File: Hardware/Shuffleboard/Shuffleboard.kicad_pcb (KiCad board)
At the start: 4 copper layers, 130 x 131.5 mm, 47 parts, among them IC1 DG3157EDL-T1-GE3, IC2 DG3157EDL-T1-GE3, J1 1869279, J2 1869279, J3 Conn_01x10, Q1 NMOS, U1 COM-09032, U2 PAM8302AAS, U3 LMV331

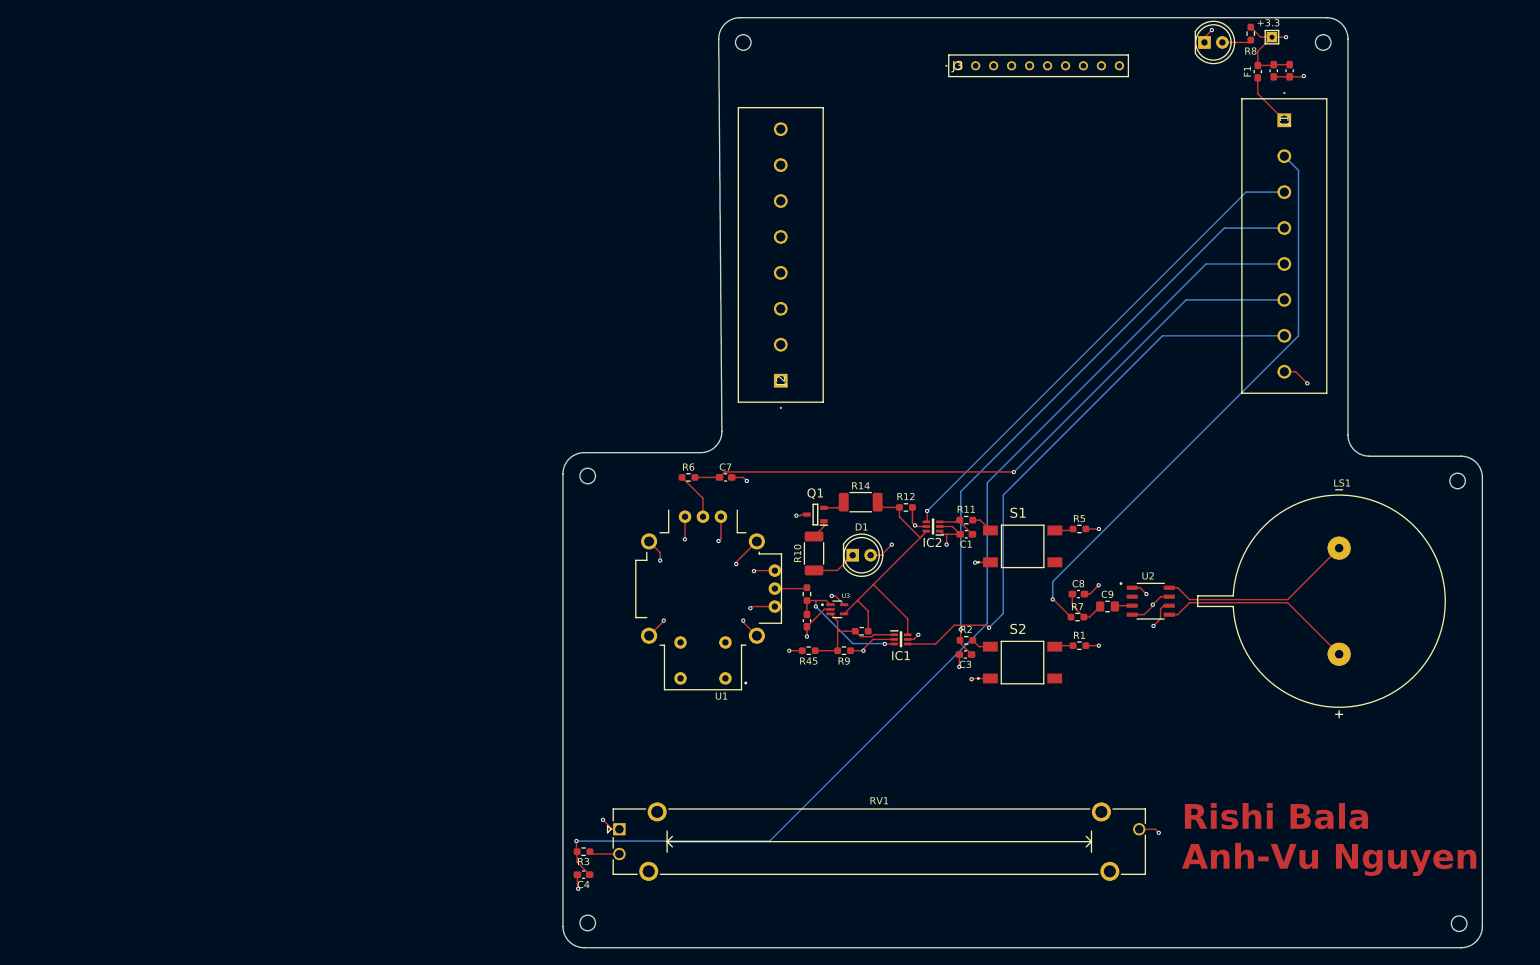
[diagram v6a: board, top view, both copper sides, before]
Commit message: footprints, tracing
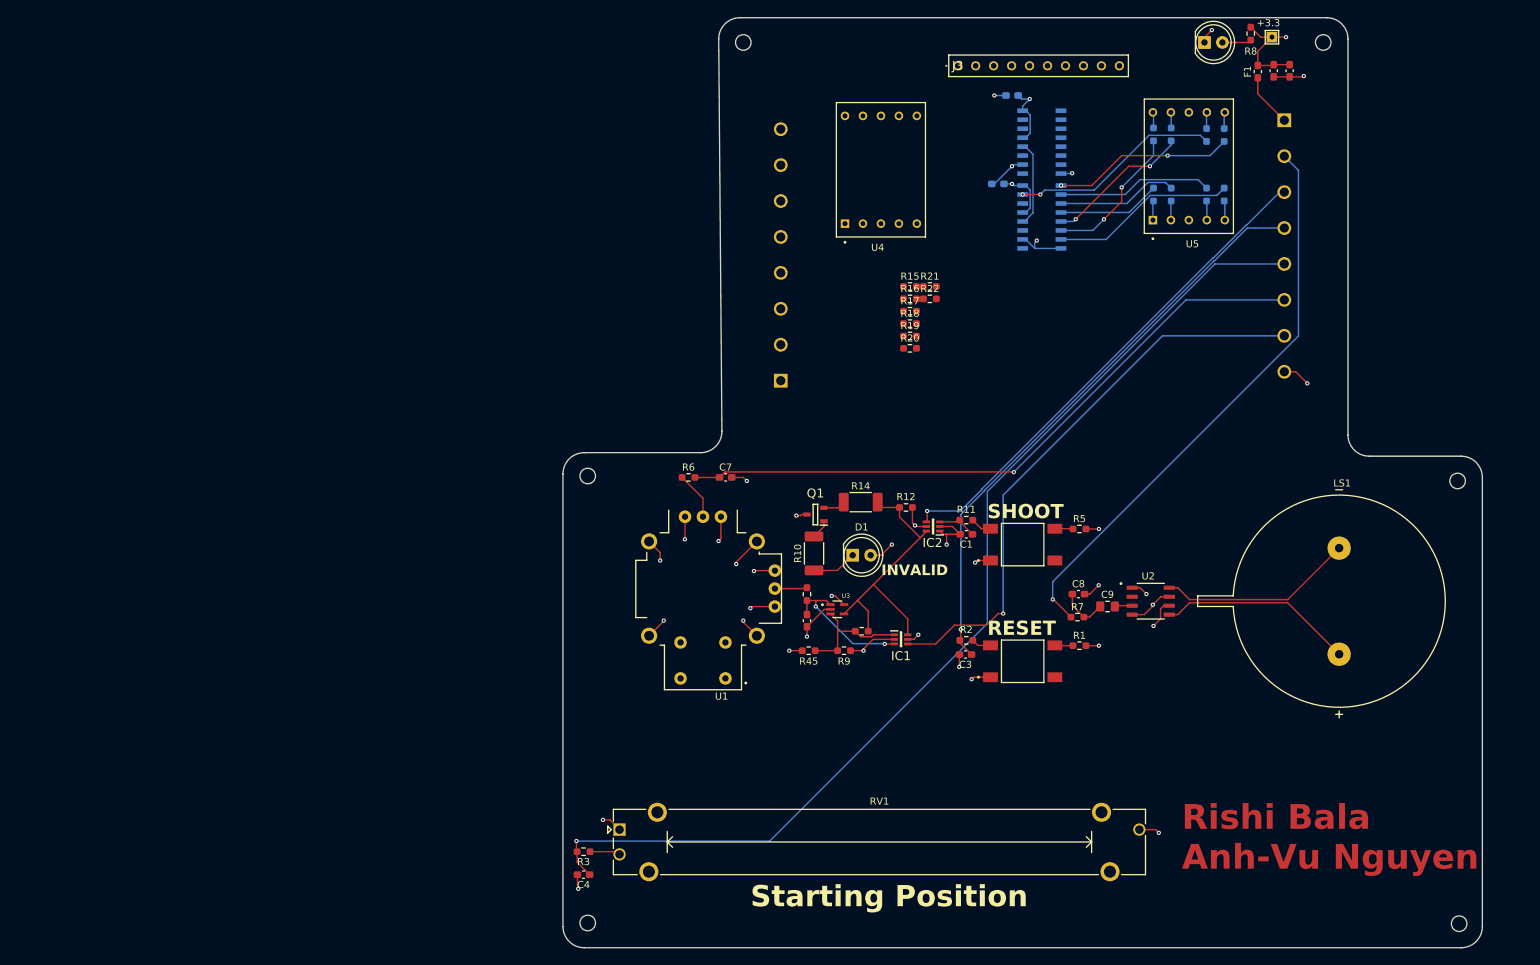
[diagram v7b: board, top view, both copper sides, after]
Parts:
- added C10: 100n, Capacitor_SMD:C_0603_1608Metric_Pad1.08x0.95mm_HandSolder, B.Cu at (173.5, 36.0)
- added C11: 100n, Capacitor_SMD:C_0603_1608Metric_Pad1.08x0.95mm_HandSolder, B.Cu at (171.5, 48.5)
- added R15: 100, Resistor_SMD:R_0603_1608Metric_Pad0.98x0.95mm_HandSolder, F.Cu at (159.1, 63.0)
- added R16: 100, Resistor_SMD:R_0603_1608Metric_Pad0.98x0.95mm_HandSolder, F.Cu at (159.1, 64.8)
- added R17: 100, Resistor_SMD:R_0603_1608Metric_Pad0.98x0.95mm_HandSolder, F.Cu at (159.1, 66.5)
- added R18: 100, Resistor_SMD:R_0603_1608Metric_Pad0.98x0.95mm_HandSolder, F.Cu at (159.1, 68.2)
- added R19: 100, Resistor_SMD:R_0603_1608Metric_Pad0.98x0.95mm_HandSolder, F.Cu at (159.1, 70.0)
- added R20: 100, Resistor_SMD:R_0603_1608Metric_Pad0.98x0.95mm_HandSolder, F.Cu at (159.1, 71.8)
- added R21: 100, Resistor_SMD:R_0603_1608Metric_Pad0.98x0.95mm_HandSolder, F.Cu at (161.9, 63.0)
- added R22: 100, Resistor_SMD:R_0603_1608Metric_Pad0.98x0.95mm_HandSolder, F.Cu at (161.9, 64.8)
- added R23: 100, Resistor_SMD:R_0603_1608Metric_Pad0.98x0.95mm_HandSolder, B.Cu at (201.0, 41.6)
- added R24: 100, Resistor_SMD:R_0603_1608Metric_Pad0.98x0.95mm_HandSolder, B.Cu at (203.5, 41.6)
- added R25: 100, Resistor_SMD:R_0603_1608Metric_Pad0.98x0.95mm_HandSolder, B.Cu at (201.0, 50.0)
- added R26: 100, Resistor_SMD:R_0603_1608Metric_Pad0.98x0.95mm_HandSolder, B.Cu at (196.0, 50.0)
- added R27: 100, Resistor_SMD:R_0603_1608Metric_Pad0.98x0.95mm_HandSolder, B.Cu at (193.5, 50.0)
- added R28: 100, Resistor_SMD:R_0603_1608Metric_Pad0.98x0.95mm_HandSolder, B.Cu at (196.0, 41.5)
- added R29: 100, Resistor_SMD:R_0603_1608Metric_Pad0.98x0.95mm_HandSolder, B.Cu at (193.5, 41.5)
- added R30: 100, Resistor_SMD:R_0603_1608Metric_Pad0.98x0.95mm_HandSolder, B.Cu at (203.5, 50.0)
- added U4: INND-TS56RCB, ShuffleboardFootprints:LED_INND-TS56RCB, F.Cu at (155.0, 46.5)
- added U5: INND-TS56RCB, ShuffleboardFootprints:LED_INND-TS56RCB, F.Cu at (198.5, 46.0)
- added U6: LOGIC-74HC595N_DIP16_, ShuffleboardFootprints:SOIC127P600X175-16N, B.Cu at (177.7, 42.6)
- added U8: LOGIC-74HC595N_DIP16_, ShuffleboardFootprints:SOIC127P600X175-16N, B.Cu at (177.7, 53.2)
- J1, J2: footprint ShuffleboardFootprints:1869279 -> Footprint:1869279; moved to B.Cu
- moved S1 0.25 mm to (175.0, 99.5)
- moved S2 0.18 mm to (175.0, 116.0)
- moved RV1 0.05 mm to (118.0, 139.8)
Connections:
- J2 pad 1: unconnected-(J2-Pad1) -> /Connector/PB8_MOSI(PICO)
- J2 pad 2: unconnected-(J2-Pad2) -> /Connector/PB9_SPI_CLK
- J2 pad 3: unconnected-(J2-Pad3) -> /Connector/PB16_LATCH_PULSE
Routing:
- net Net-(U8-QA): track 0.00 -> 29.8 mm, vias 0 -> 2
- net Net-(U8-QH): track 0.00 -> 26.1 mm
- net Net-(U8-QB): track 0.00 -> 25.7 mm, vias 0 -> 2
- net Net-(U8-QC): track 0.00 -> 21.9 mm
- net Net-(U8-QG): track 0.00 -> 20.7 mm, vias 0 -> 2
- net Net-(U8-QF): track 0.00 -> 20.6 mm, vias 0 -> 2
- net +3.3V: track 50.3 -> 67.6 mm, vias 13 -> 15
- net Net-(U8-QD): track 0.00 -> 17.1 mm
- net GND: track 74.2 -> 90.1 mm, vias 21 -> 25
- net Net-(U8-QE): track 0.00 -> 14.5 mm
- net /7Seg/PB16_LATCH_PULSE: track 0.00 -> 12.2 mm
- net Net-(R30-Pad2): track 0.00 -> 2.74 mm
- net Net-(R27-Pad2): track 0.00 -> 2.74 mm
- net Net-(R26-Pad2): track 0.00 -> 2.72 mm
- net Net-(R25-Pad2): track 0.00 -> 2.72 mm
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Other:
- board text added: "INVALID"
- board text added: "RESET"
- board text added: "SHOOT"
- board text added: "Starting Position"

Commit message: layout prep
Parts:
- R15, R16, R17, R18, R19, R20, R21, R22: moved to B.Cu
- moved R15 2.81 mm to (161.9, 63.0), turned to 180 degrees
- moved R16 2.81 mm to (161.9, 64.8), turned to 180 degrees
- moved R17 2.81 mm to (161.9, 66.5), turned to 180 degrees
- moved R18 2.81 mm to (161.9, 68.2), turned to 180 degrees
- moved R19 2.81 mm to (161.9, 70.0), turned to 180 degrees
- moved R20 2.81 mm to (161.9, 71.8), turned to 180 degrees
- moved R21 2.81 mm to (159.1, 63.0), turned to 180 degrees
- moved R22 2.81 mm to (159.1, 64.8), turned to 180 degrees
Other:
- board text added: "Power"
